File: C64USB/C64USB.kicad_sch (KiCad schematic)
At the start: 32 parts, among them J2 USB_B, J3 AVR-ISP-6, J4 Joystick1, J5 Joystick2, J6 LED, U2 ATmega88-20A, Y1 16MHz

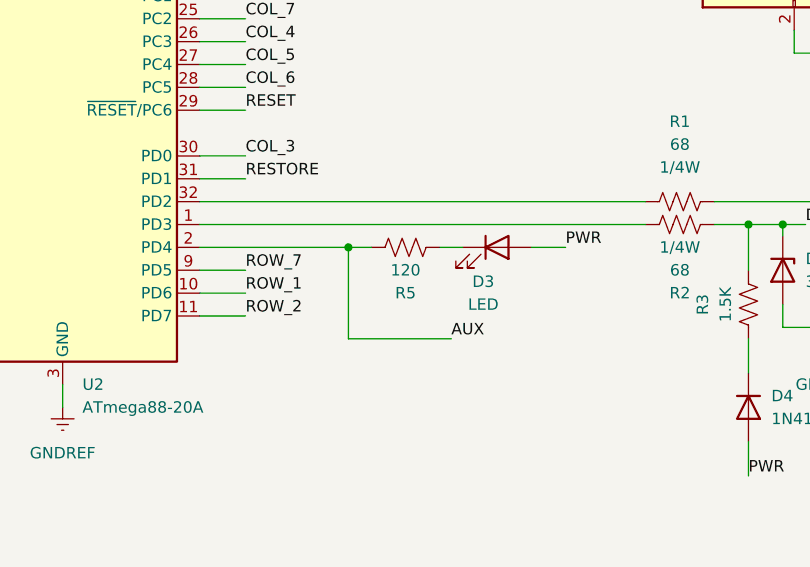
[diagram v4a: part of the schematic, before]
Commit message: Remove debug LED
The debug LED isn't particularly useful since it's tied to the AUX line
and I didn't even bother populating it on the prototype board
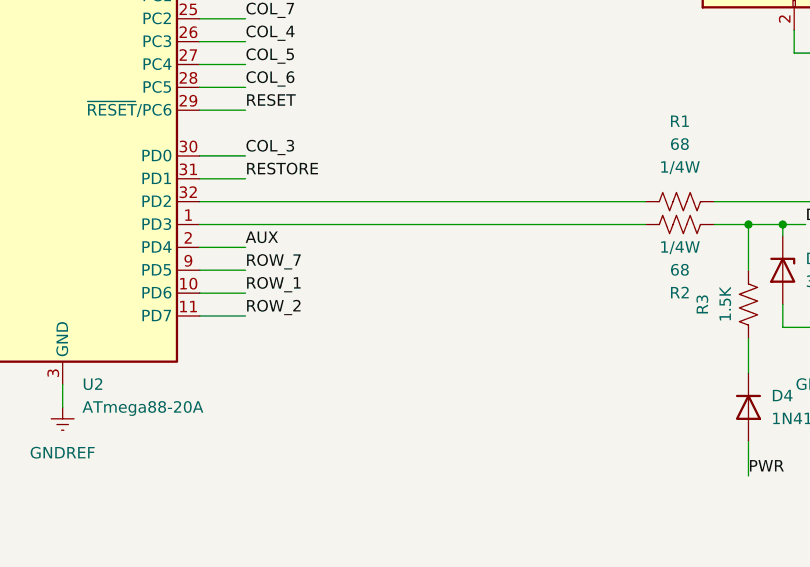
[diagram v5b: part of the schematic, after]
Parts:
- removed D3: LED, LED_SMD:LED_0603_1608Metric, symbol Device:LED
- removed R5: 120, Resistor_SMD:R_0603_1608Metric_Pad0.98x0.95mm_HandSolder, symbol Device:R_US
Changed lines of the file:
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@@
 	)
 	(junction
-		(at 203.2 119.38)
-		(diameter 0)
-		(color 0 0 0 0)
-	)
-	(junction
 		(at 262.89 33.02)
 		(diameter 0)
@@
 	(wire
 		(pts
-			(xy 203.2 119.38) (xy 205.74 119.38)
-		)
-		(stroke
-			(width 0)
-			(type default)
-		)
-	)
-	(wire
-		(pts
 			(xy 243.84 114.3) (xy 261.62 114.3)
 		)
@@
 	(wire
 		(pts
-			(xy 203.2 129.54) (xy 203.2 119.38)
-		)
-		(stroke
-			(width 0)
-			(type default)
-		)
-	)
-	(wire
-		(pts
 			(xy 247.65 25.4) (xy 243.84 25.4)
 		)
@@
 	(wire
 		(pts
-			(xy 214.63 129.54) (xy 203.2 129.54)
-		)
-		(stroke
-			(width 0)
-			(type default)
-		)
-	)
-	(wire
-		(pts
 			(xy 50.8 144.78) (xy 73.66 144.78)
 		)
@@
 	(wire
 		(pts
-			(xy 223.52 119.38) (xy 227.33 119.38)
-		)
-		(stroke
-			(width 0)
-			(type default)
-		)
-	)
-	(wire
-		(pts
 			(xy 50.8 182.88) (xy 55.88 182.88)
 		)
@@
 	(wire
 		(pts
-			(xy 213.36 119.38) (xy 215.9 119.38)
-		)
-		(stroke
-			(width 0)
-			(type default)
-		)
-	)
-	(wire
-		(pts
 			(xy 171.45 134.62) (xy 171.45 137.16)
 		)
@@
 	(wire
 		(pts
+			(xy 186.69 119.38) (xy 191.77 119.38)
+		)
+		(stroke
+			(width 0)
+			(type default)
+		)
+	)
+	(wire
+		(pts
 			(xy 213.36 46.99) (xy 224.79 46.99)
 		)
@@
 	(wire
 		(pts
-			(xy 186.69 119.38) (xy 203.2 119.38)
-		)
-		(stroke
-			(width 0)
-			(type default)
-		)
-	)
-	(wire
-		(pts
 			(xy 186.69 68.58) (xy 191.77 68.58)
 		)
@@
 	)
 	(label "AUX"
-		(at 214.63 129.54 0)
+		(at 191.77 119.38 0)
 		(fields_autoplaced yes)
 		(effects
@@
 		)
 	)
-	(label "PWR"
-		(at 227.33 119.38 0)
-		(fields_autoplaced yes)
-		(effects
-			(font
-				(size 1.27 1.27)
-			)
-			(justify left bottom)
-		)
-	)
 	(label "ROW_7"
 		(at 191.77 121.92 0)
@@
 	)
 	(symbol
-		(lib_id "Device:LED")
-		(at 219.71 119.38 0)
-		(unit 1)
-		(exclude_from_sim no)
-		(in_bom yes)
-		(on_board yes)
-		(dnp no)
-		(property "Reference" "D3"
-			(at 218.186 123.19 0)
-			(effects
-				(font
-					(size 1.27 1.27)
-				)
-			)
-		)
-		(property "Value" "LED"
-			(at 218.186 125.73 0)
-			(effects
-				(font
-					(size 1.27 1.27)
-				)
-			)
-		)
-		(property "Footprint" "LED_SMD:LED_0603_1608Metric"
-			(at 219.71 119.38 0)
-			(effects
-				(font
-					(size 1.27 1.27)
-				)
-				(hide yes)
-			)
-		)
-		(property "Datasheet" "~"
-			(at 219.71 119.38 0)
-			(effects
-				(font
-					(size 1.27 1.27)
-				)
-				(hide yes)
-			)
-		)
-		(property "Description" "Light emitting diode"
-			(at 219.71 119.38 0)
-			(effects
-				(font
-					(size 1.27 1.27)
-				)
-				(hide yes)
-			)
-		)
-		(pin "1"
-		)
-		(pin "2"
-		)
-		(instances
-			(project ""
-				(path "/683b04d7-2177-49fe-8cac-bb0e8fe56ae0"
-					(reference "D3")
-					(unit 1)
-				)
-			)
-		)
-	)
-	(symbol
 		(lib_id "power:GNDREF")
 		(at 213.36 49.53 0)
@@
 					(unit 1)
 				)
-			)
-		)
-	)
-	(symbol
-		(lib_id "Device:R_US")
-		(at 209.55 119.38 90)
-		(unit 1)
-		(exclude_from_sim no)
-		(in_bom yes)
-		(on_board yes)
-		(dnp no)
-		(property "Reference" "R5"
-			(at 209.55 124.46 90)
-			(effects
-				(font
-					(size 1.27 1.27)
-				)
-			)
-		)
-		(property "Value" "120"
-			(at 209.55 121.92 90)
-			(effects
-				(font
-					(size 1.27 1.27)
-				)
-			)
-		)
-		(property "Footprint" "Resistor_SMD:R_0603_1608Metric_Pad0.98x0.95mm_HandSolder"
-			(at 209.804 118.364 90)
-			(effects
-				(font
-					(size 1.27 1.27)
-				)
-				(hide yes)
-			)
-		)
-		(property "Datasheet" "~"
-			(at 209.55 119.38 0)
-			(effects
-				(font
-					(size 1.27 1.27)
-				)
-				(hide yes)
-			)
-		)
-		(property "Description" "Resistor, US symbol"
-			(at 209.55 119.38 0)
-			(effects
-				(font
-					(size 1.27 1.27)
-				)
-				(hide yes)
-			)
-		)
-		(pin "2"
-		)
-		(pin "1"
-		)
-		(instances
-			(project "C64USB"
-				(path "/683b04d7-2177-49fe-8cac-bb0e8fe56ae0"
-					(reference "R5")
-					(unit 1)
-				)

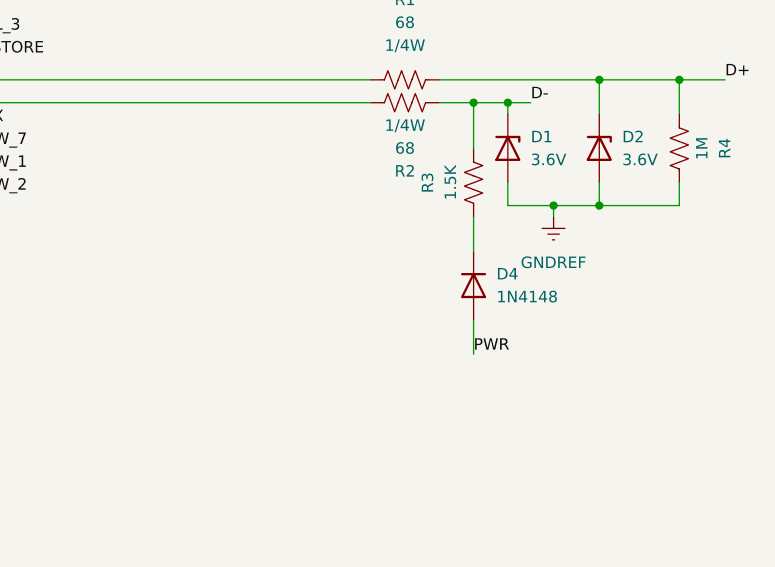
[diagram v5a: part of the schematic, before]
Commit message: Back Power Protection Diode
Some USB host controller (specifically, the one on the Raspberry Pi 4)
can detect if a device is being back powered through the D+ line (that
is, drawing power through D+ when the 5V supply is off), and if so will
shut down the port. Add a diode on the D+ line to prevent power from
being drawn through it.
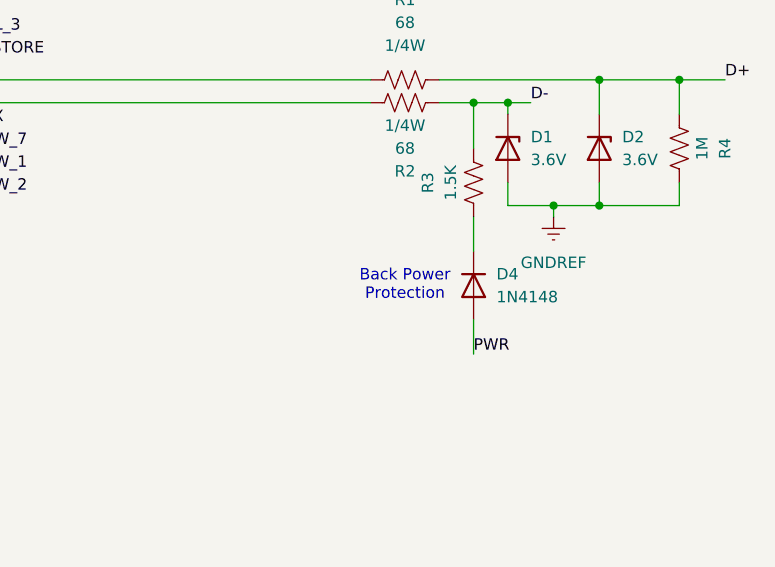
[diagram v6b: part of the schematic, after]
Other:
- note added: "Back Power Protection"
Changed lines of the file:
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@@
+		)
+	)
+	(text "Back Power\nProtection"
+		(exclude_from_sim no)
+		(at 240.03 137.16 0)
+		(effects
+			(font
+				(size 1.27 1.27)
+			)
 		)
 	)

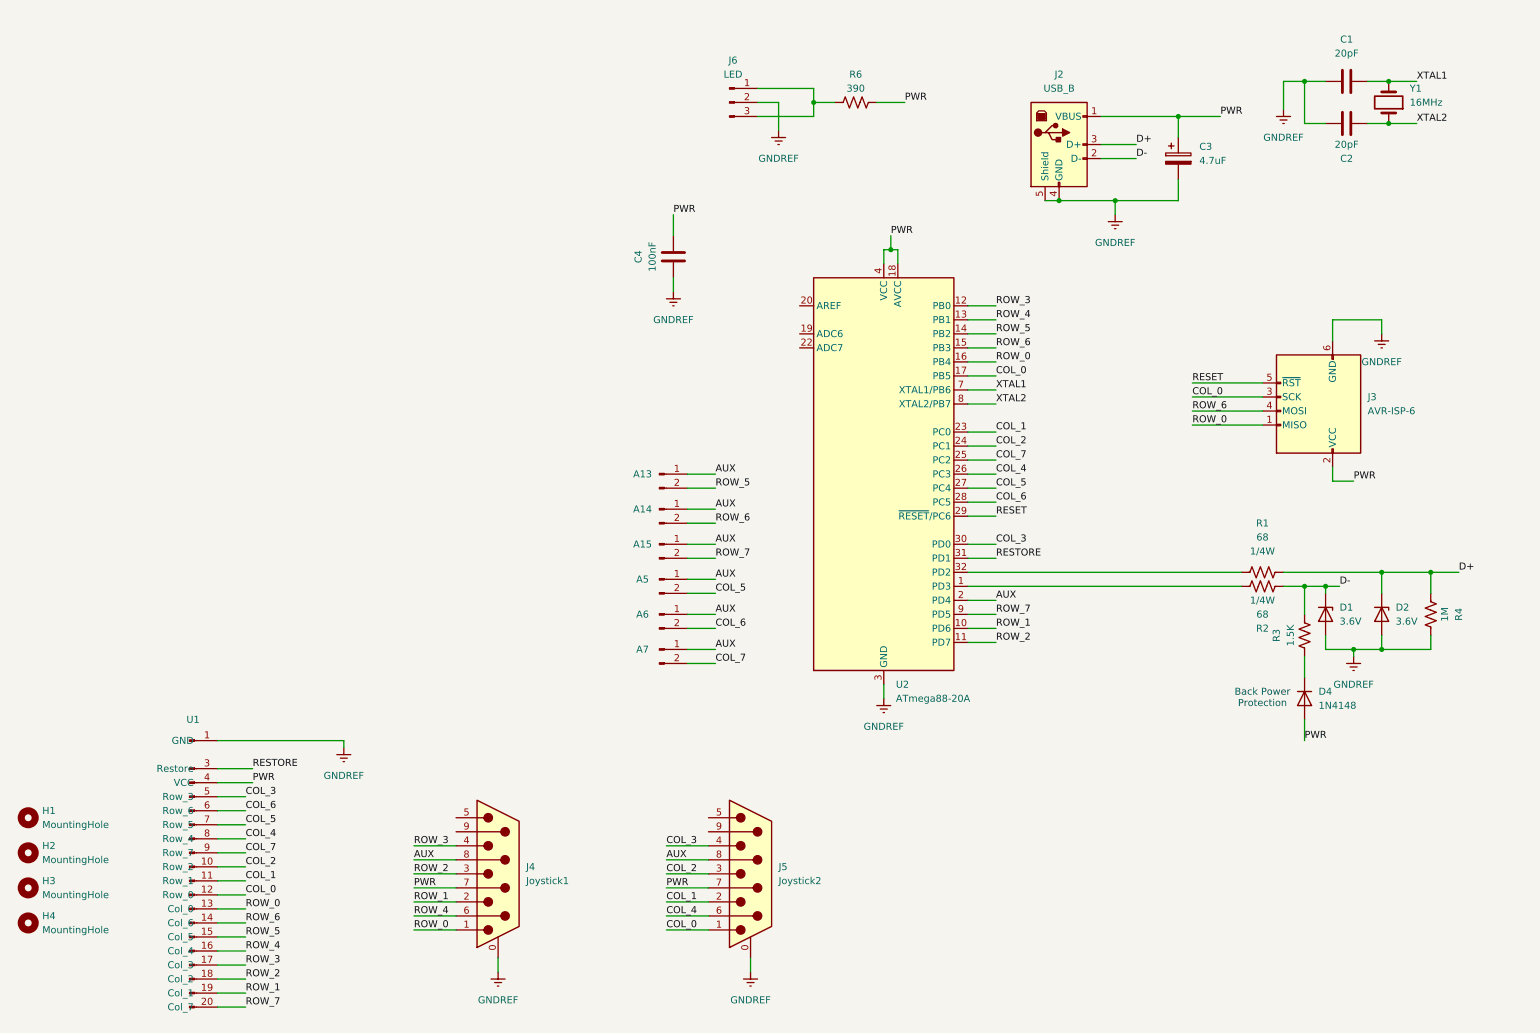
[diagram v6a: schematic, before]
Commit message: Use buffer on joystick and aux keys
There was a problem where joystick or auxiliary key inputs would result
in keyboard keys being detected when they were not actually pressed.
While this is accurate to the actual Commodore 64 keyboard and joystick
input, having it happen on this USB device meant that it could not be
correctly disambiguated by the emulator. As such, the board is
redesigned to use a 74HCT541 tri state buffer chip to isolate the
Joystick and auxiliary inputs from the keyboard. It is still possible
that keyboard inputs can incorrectly show up as joystick movement, but
this is much less likely to cause a problem.

With the board redesign, the clearance around the keyboard header was
also increased to allow it to fit, and the USB connector was changed
from a micro-USB connector to a USB-B connector (I had too much trouble
hand soldering the micro USB connector).
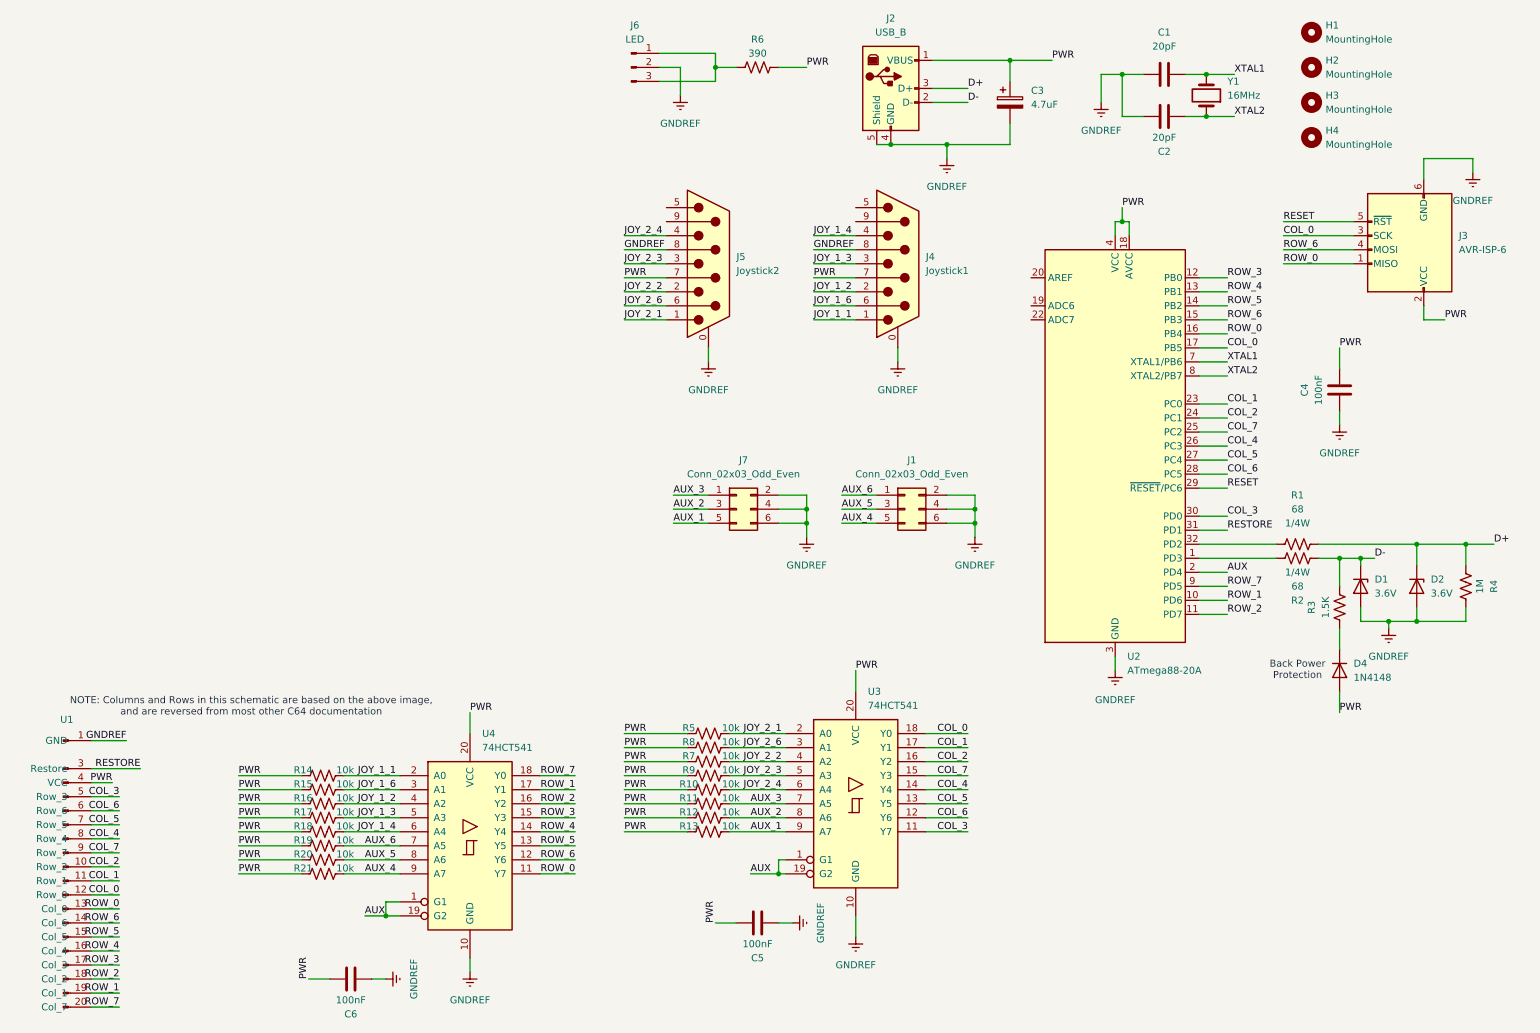
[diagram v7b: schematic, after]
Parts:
- removed A13, A14, A15, A5, A6, A7: ~, Connector_PinHeader_2.54mm:PinHeader_1x02_P2.54mm_Vertical, symbol Connector:Conn_01x02_Pin
- added C5, C6: 100nF, Capacitor_SMD:C_0603_1608Metric_Pad1.08x0.95mm_HandSolder, symbol Device:C
- added J1, J7: Conn_02x03_Odd_Even, Connector_PinHeader_2.54mm:PinHeader_2x03_P2.54mm_Vertical, symbol Connector_Generic:Conn_02x03_Odd_Even
- added R10, R11, R12, R13, R14, R15, R16, R17, R18, R19, R20, R21, R5, R7, R8, R9: 10k, Resistor_SMD:R_0603_1608Metric_Pad0.98x0.95mm_HandSolder, symbol Device:R_US
- added U3, U4: 74HCT541, Package_SO:SOIC-20W_7.5x12.8mm_P1.27mm, symbol 74xx:74HCT541
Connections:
- net AUX: now also U3.1 (G1), U3.19 (G2), U4.1 (G1), U4.19 (G2); no longer J4.8, J5.8
- net COL_0: now also U3.18 (Y0); no longer J5.1
- net COL_1: now also U3.17 (Y1); no longer J5.2
- net COL_2: now also U3.16 (Y2); no longer J5.3
- net COL_3: now also U3.11 (Y7); no longer J5.4
- net COL_4: now also U3.14 (Y4); no longer J5.6
- net COL_5: now also U3.13 (Y5)
- net COL_6: now also U3.12 (Y6)
- net COL_7: now also U3.15 (Y3)
- net GNDREF: now also J4.8, J5.8, C5.2, C6.2, J1.2 (Pin_2), J1.4 (Pin_4), J1.6 (Pin_6), J7.2 (Pin_2), J7.4 (Pin_4), J7.6 (Pin_6), U3.10 (GND), U4.10 (GND)
- net PWR: now also C5.1, C6.1, R10.1, R11.1, R12.1, R13.1, R14.1, R15.1, R16.1, R17.1, R18.1, R19.1, R20.1, R21.1, R5.1, R7.1, R8.1, R9.1, U3.20 (VCC), U4.20 (VCC)
- net ROW_0: now also U4.11 (Y7); no longer J4.1
- net ROW_1: now also U4.17 (Y1); no longer J4.2
- net ROW_2: now also U4.16 (Y2); no longer J4.3
- net ROW_3: now also U4.15 (Y3); no longer J4.4
- net ROW_4: now also U4.14 (Y4); no longer J4.6
- net ROW_5: now also U4.13 (Y5)
- net ROW_6: now also U4.12 (Y6)
- net ROW_7: now also U4.18 (Y0)
- new net AUX_1: J7.5 (Pin_5), R13.2, U3.9 (A7)
- new net AUX_2: J7.3 (Pin_3), R12.2, U3.8 (A6)
- new net AUX_3: J7.1 (Pin_1), R11.2, U3.7 (A5)
- new net AUX_4: J1.5 (Pin_5), R21.2, U4.9 (A7)
- new net AUX_5: J1.3 (Pin_3), R20.2, U4.8 (A6)
- new net AUX_6: J1.1 (Pin_1), R19.2, U4.7 (A5)
- new net JOY_1_1: J4.1, R14.2, U4.2 (A0)
- new net JOY_1_2: J4.2, R16.2, U4.4 (A2)
- new net JOY_1_3: J4.3, R17.2, U4.5 (A3)
- new net JOY_1_4: J4.4, R18.2, U4.6 (A4)
- new net JOY_1_6: J4.6, R15.2, U4.3 (A1)
- new net JOY_2_1: J5.1, R5.2, U3.2 (A0)
- new net JOY_2_2: J5.2, R7.2, U3.4 (A2)
- new net JOY_2_3: J5.3, R9.2, U3.5 (A3)
- new net JOY_2_4: J5.4, R10.2, U3.6 (A4)
- new net JOY_2_6: J5.6, R8.2, U3.3 (A1)
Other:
- note added: "NOTE: Columns and Rows in this schematic are based on the above image, and are reversed from most other C64 documentation"
- moved on the sheet: C1, C2, C3, C4, D1, D2, D4, H1, H2, H3, H4, J2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
